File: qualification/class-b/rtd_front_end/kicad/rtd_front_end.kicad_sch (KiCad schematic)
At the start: 12 parts, among them U1 LM358

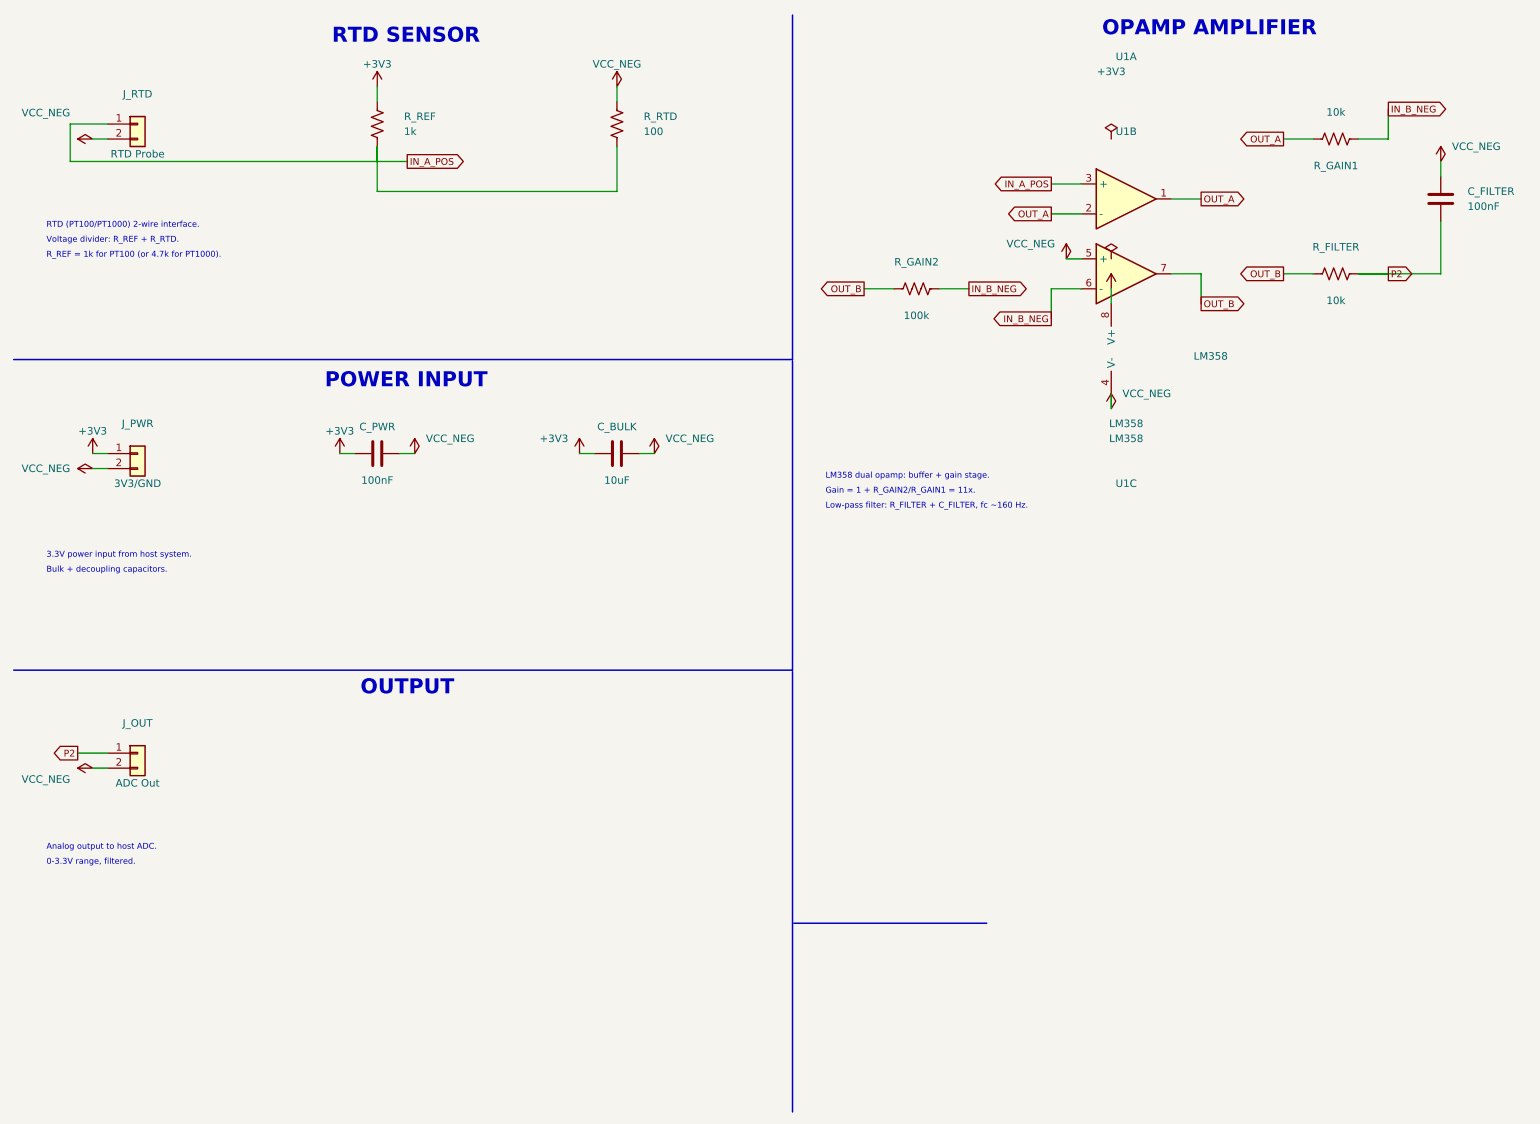
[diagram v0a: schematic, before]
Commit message: fix: address PR review - restructure as qualification boards, fix RTD topology, USB ESD, BME280 (SYN-365)
Changes:
- Move from examples/ to qualification/class-b/<board>/ with README, SHA256SUMS, qualification.json
- Fix RTD amplifier: non-inverting gain stage (1+R2/R1=11x) instead of inverting
- Fix USB ESD: separate D_ESD_DP and D_ESD_DN diodes instead of shorting D+/D-
- Add BME280 part to registry (issue specifies BME280, not BME680)
- Add i2c_sda/i2c_scl capabilities to nrf52840 p0_06/p0_08
- Fix balun_2g4 footprint to real KiCad part
- Re-route BLE node: 0 unconnected pads (manual via-in-pad escape)
- Add DRC/ERC reports, SHA256SUMS, qualification.json for both boards
- Remove silkscreen labels, add USB-C 3D model reference
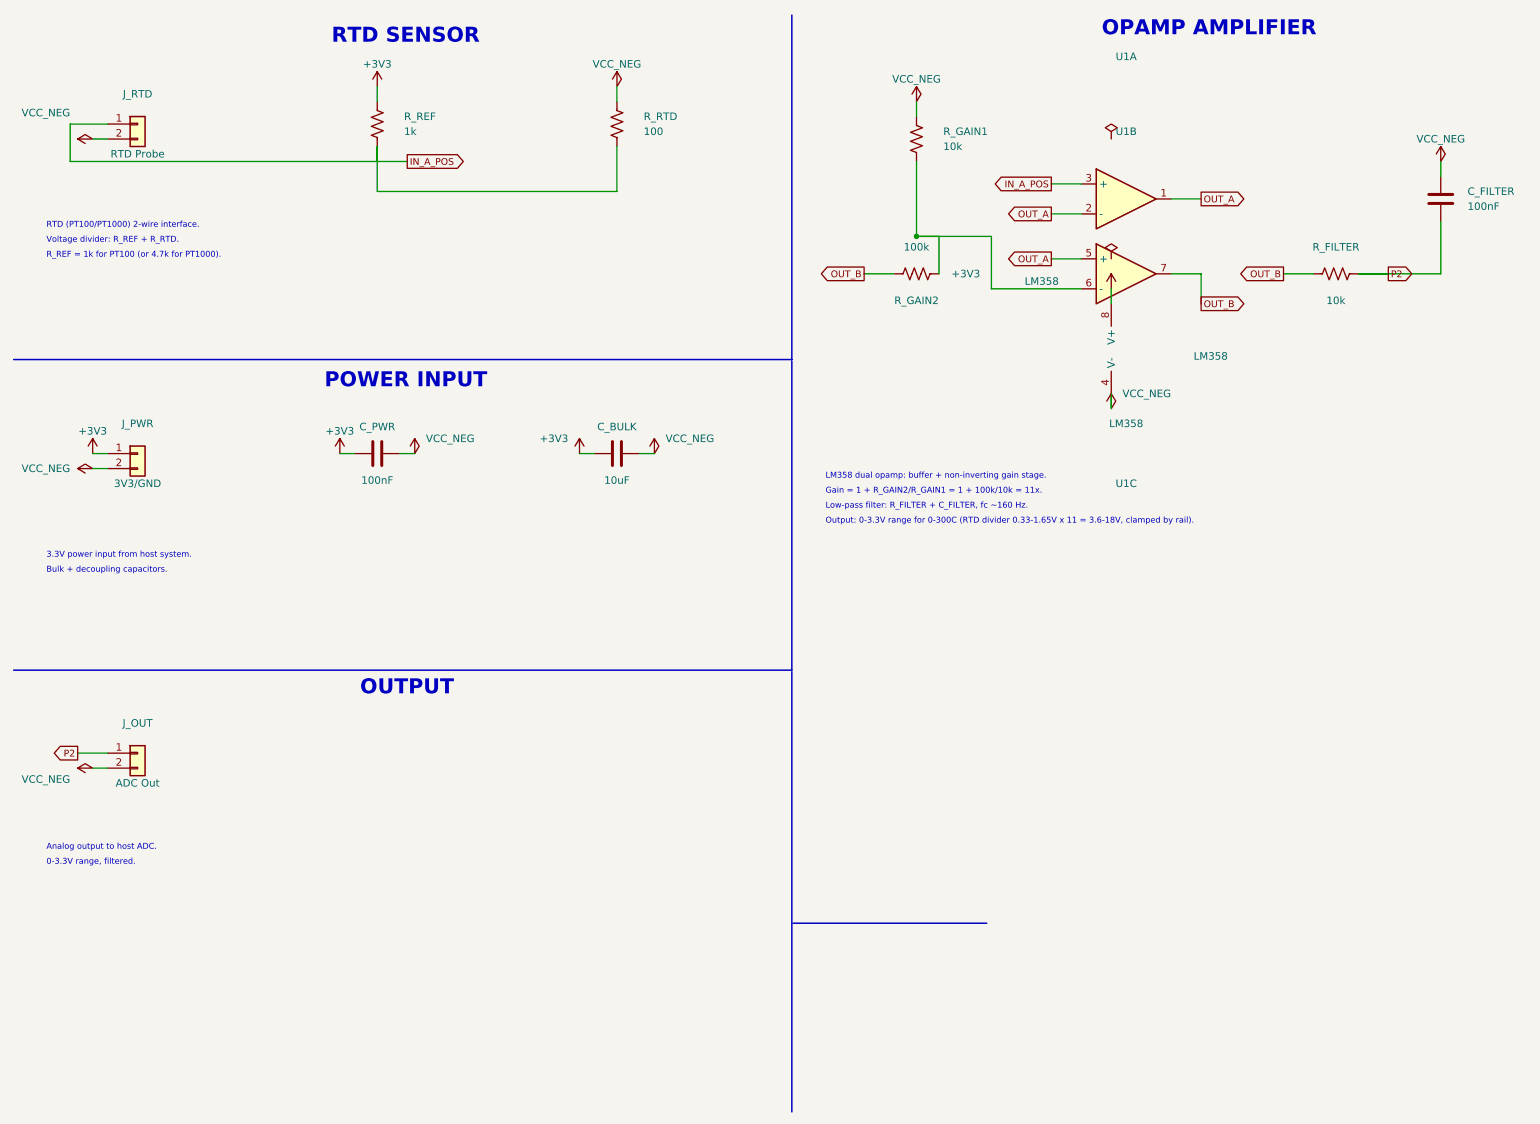
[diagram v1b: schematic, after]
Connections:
- net OUT_A: now also U1.5 (+); no longer R_GAIN1.1
- net VCC_NEG: now also R_GAIN1.2; no longer U1.5 (+)
- net IN_B_NEG: no longer names the net of R_GAIN2.1, U1.6 (-)
- net IN_B_NEG: now also R_GAIN1.1; no longer R_GAIN1.2
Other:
- note added: "Gain = 1 + R_GAIN2/R_GAIN1 = 1 + 100k/10k = 11x."
- note added: "LM358 dual opamp: buffer + non-inverting gain stage."
- note added: "Output: 0-3.3V range for 0-300C (RTD divider 0.33-1.65V x 11 = 3.6-18V, clamped by rail)."
- note removed: "Gain = 1 + R_GAIN2/R_GAIN1 = 11x."
- note removed: "LM358 dual opamp: buffer + gain stage."
- moved on the sheet: R_GAIN1, R_GAIN2
